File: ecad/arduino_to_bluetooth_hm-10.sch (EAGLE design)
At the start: 4 parts

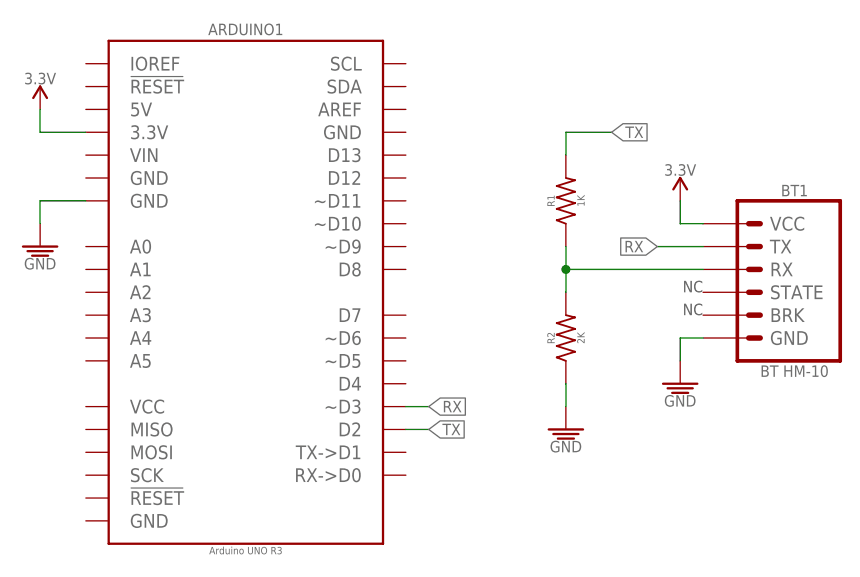
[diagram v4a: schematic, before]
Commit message: Small adjustment to schematic naming.  Update image to reflect changes in schematic.
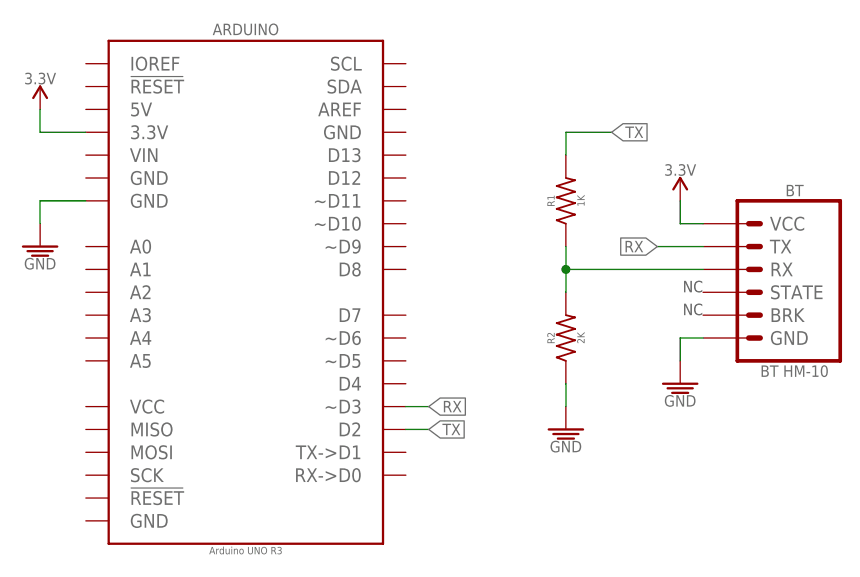
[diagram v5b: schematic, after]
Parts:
- renumbered ARDUINO1 to ARDUINO, BT1 to BT
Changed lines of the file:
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@@
 </classes>
 <parts>
-<part name="ARDUINO1" library="PiB_boards" deviceset="ARDUINO_UNO_R3" device="" value="Arduino UNO R3"/>
-<part name="BT1" library="PiB_radio_frequency" deviceset="BLUETOOTH_HM-10" device="1X06-RA-FEMALE" value="BT HM-10"/>
+<part name="ARDUINO" library="PiB_boards" deviceset="ARDUINO_UNO_R3" device="" value="Arduino UNO R3"/>
+<part name="BT" library="PiB_radio_frequency" deviceset="BLUETOOTH_HM-10" device="1X06-RA-FEMALE" value="BT HM-10"/>
 <part name="SUPPLY1" library="PiB_power_symbols" deviceset="GND" device=""/>
 <part name="SUPPLY2" library="PiB_power_symbols" deviceset="GND" device=""/>
@@
 </plain>
 <instances>
-<instance part="ARDUINO1" gate="G$1" x="48.26" y="50.8"/>
-<instance part="BT1" gate="G$1" x="109.22" y="53.34" rot="MR0"/>
+<instance part="ARDUINO" gate="G$1" x="48.26" y="50.8"/>
+<instance part="BT" gate="G$1" x="109.22" y="53.34" rot="MR0"/>
 <instance part="SUPPLY1" gate="GND" x="25.4" y="55.88"/>
 <instance part="SUPPLY2" gate="GND" x="96.52" y="40.64"/>
@@
 <net name="RX" class="0">
 <segment>
-<pinref part="BT1" gate="G$1" pin="RX"/>
+<pinref part="BT" gate="G$1" pin="RX"/>
 <wire x1="99.06" y1="53.34" x2="83.82" y2="53.34" width="0.1524" layer="91"/>
 <pinref part="R2" gate="G$1" pin="2"/>
@@
 </segment>
 <segment>
-<pinref part="ARDUINO1" gate="G$1" pin="~D3"/>
+<pinref part="ARDUINO" gate="G$1" pin="~D3"/>
 <wire x1="68.58" y1="38.1" x2="66.04" y2="38.1" width="0.1524" layer="91"/>
 <label x="68.58" y="38.1" size="1.27" layer="95" ratio="10" xref="yes"/>
 </segment>
 <segment>
-<pinref part="BT1" gate="G$1" pin="TX"/>
+<pinref part="BT" gate="G$1" pin="TX"/>
 <wire x1="99.06" y1="55.88" x2="93.98" y2="55.88" width="0.1524" layer="91"/>
 <label x="93.98" y="55.88" size="1.27" layer="95" ratio="10" rot="R180" xref="yes"/>
@@
 <net name="GND" class="0">
 <segment>
-<pinref part="ARDUINO1" gate="G$1" pin="GND@1"/>
+<pinref part="ARDUINO" gate="G$1" pin="GND@1"/>
 <wire x1="30.48" y1="60.96" x2="25.4" y2="60.96" width="0.1524" layer="91"/>
 <wire x1="25.4" y1="60.96" x2="25.4" y2="58.42" width="0.1524" layer="91"/>
@@
 </segment>
 <segment>
-<pinref part="BT1" gate="G$1" pin="GND"/>
+<pinref part="BT" gate="G$1" pin="GND"/>
 <wire x1="99.06" y1="45.72" x2="96.52" y2="45.72" width="0.1524" layer="91"/>
 <wire x1="96.52" y1="45.72" x2="96.52" y2="43.18" width="0.1524" layer="91"/>
@@
 <net name="3.3V" class="0">
 <segment>
-<pinref part="BT1" gate="G$1" pin="VCC"/>
+<pinref part="BT" gate="G$1" pin="VCC"/>
 <wire x1="99.06" y1="58.42" x2="96.52" y2="58.42" width="0.1524" layer="91"/>
 <wire x1="96.52" y1="58.42" x2="96.52" y2="60.96" width="0.1524" layer="91"/>
@@
 </segment>
 <segment>
-<pinref part="ARDUINO1" gate="G$1" pin="3.3V"/>
+<pinref part="ARDUINO" gate="G$1" pin="3.3V"/>
 <wire x1="30.48" y1="68.58" x2="25.4" y2="68.58" width="0.1524" layer="91"/>
 <wire x1="25.4" y1="68.58" x2="25.4" y2="71.12" width="0.1524" layer="91"/>
@@
 </segment>
 <segment>
-<pinref part="ARDUINO1" gate="G$1" pin="D2"/>
+<pinref part="ARDUINO" gate="G$1" pin="D2"/>
 <wire x1="68.58" y1="35.56" x2="66.04" y2="35.56" width="0.1524" layer="91"/>
 <label x="68.58" y="35.56" size="1.27" layer="95" ratio="10" xref="yes"/>

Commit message: One last small change to schematic and export image.
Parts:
- BT: value BT HM-10 -> HM-10
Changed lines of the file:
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@@
 <setting verticaltext="up"/>
 </settings>
-<grid distance="0.1" unitdist="inch" unit="inch" style="lines" multiple="1" display="no" altdistance="0.5" altunitdist="inch" altunit="inch"/>
+<grid distance="0.1" unitdist="inch" unit="inch" style="lines" multiple="1" display="no" altdistance="0.01" altunitdist="inch" altunit="inch"/>
 <layers>
 <layer number="1" name="Top" color="4" fill="1" visible="no" active="no"/>
@@
 <parts>
 <part name="ARDUINO" library="PiB_boards" deviceset="ARDUINO_UNO_R3" device="" value="Arduino UNO R3"/>
-<part name="BT" library="PiB_radio_frequency" deviceset="BLUETOOTH_HM-10" device="1X06-RA-FEMALE" value="BT HM-10"/>
+<part name="BT" library="PiB_radio_frequency" deviceset="BLUETOOTH_HM-10" device="1X06-RA-FEMALE" value="HM-10"/>
 <part name="SUPPLY1" library="PiB_power_symbols" deviceset="GND" device=""/>
 <part name="SUPPLY2" library="PiB_power_symbols" deviceset="GND" device=""/>
